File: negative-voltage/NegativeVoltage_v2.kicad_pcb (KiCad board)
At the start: 2 copper layers, 53.3 x 69.9 mm, 11 parts, among them J1 Screw_Terminal_01x02, J2 Screw_Terminal_01x02, U1 LM555

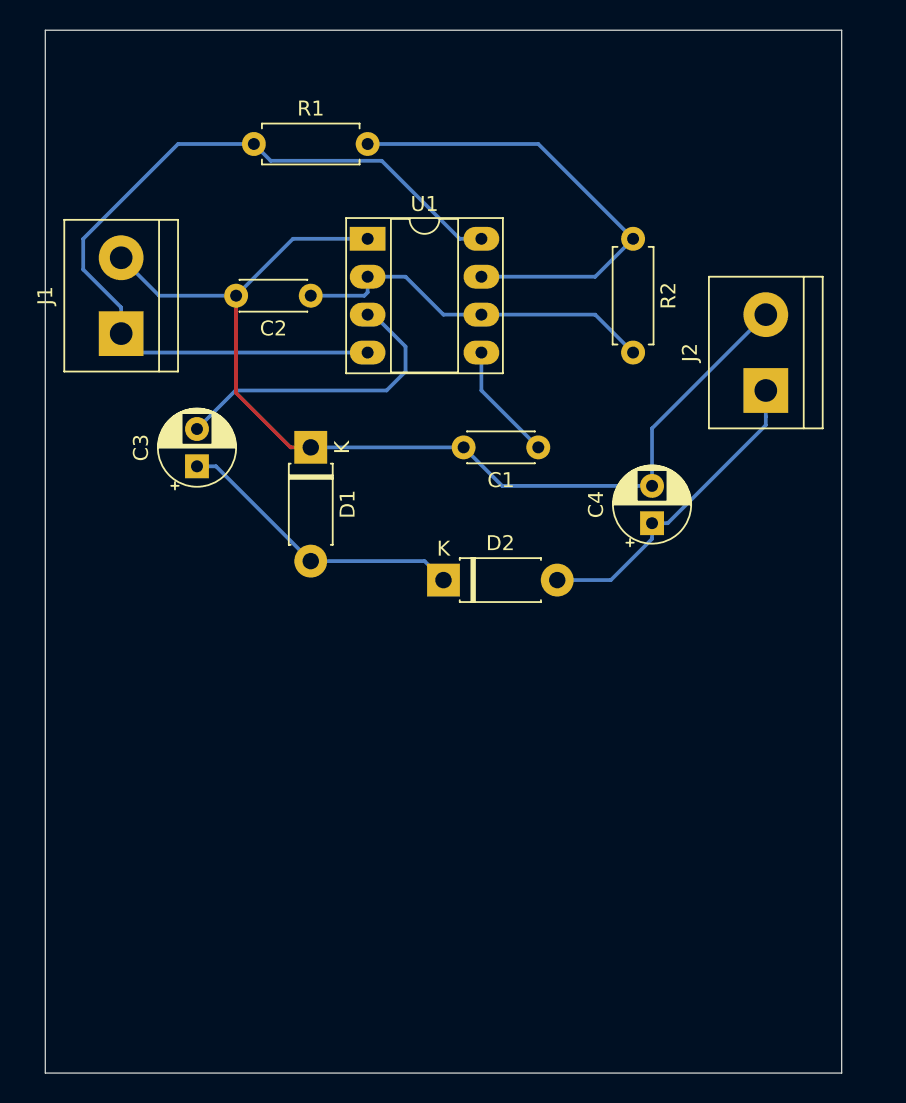
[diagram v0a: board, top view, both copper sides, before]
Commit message: Add second version with only one sided routing
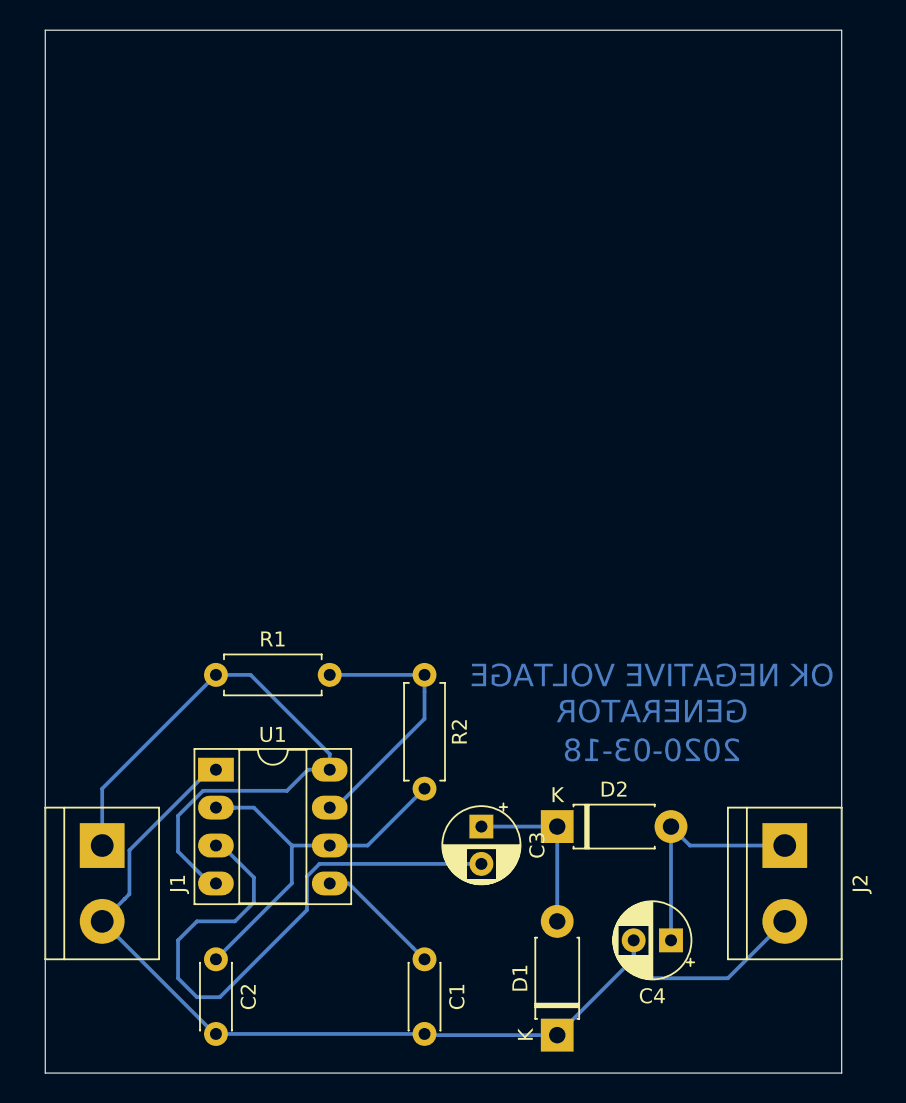
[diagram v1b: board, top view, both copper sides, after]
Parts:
- moved C2 44.9 mm to (62.2, 154.9), turned to 270 degrees
- moved D1 42.7 mm to (85.1, 160.0), turned to 90 degrees
- moved U1 37.0 mm to (62.2, 142.2)
- moved R1 35.7 mm to (62.2, 135.9)
- moved C1 35.1 mm to (76.2, 154.9), turned to 270 degrees
- moved J1 34.3 mm to (54.6, 147.3), turned to 270 degrees
- moved R2 32.4 mm to (76.2, 135.9)
- moved C3 30.7 mm to (80.0, 146.1), turned to 270 degrees
- moved J2 30.5 mm to (100.3, 147.3), turned to 270 degrees
- moved C4 28.0 mm to (92.7, 153.7), turned to 180 degrees
- moved D2 18.2 mm to (85.1, 146.1)
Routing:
- net N$4: track 20.7 -> 39.6 mm
- net VCC: track 56.4 -> 42.7 mm
- net N$3: track 31.6 -> 18.1 mm
- net N$5: track 19.7 -> 11.4 mm
- net N$6: track 21.2 -> 15.8 mm
- net N$1: track 24.8 -> 28.0 mm
- net GND: track 70.7 -> 69.2 mm
- net N$2: track 7.93 -> 8.45 mm
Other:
- board text added: "2020-03-18"
- board text added: "OK NEGATIVE VOLTAGE GENERATOR"
